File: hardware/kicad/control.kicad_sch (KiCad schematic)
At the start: 5 parts, among them SW1 MIDI channel, U9 Teensy 4.0

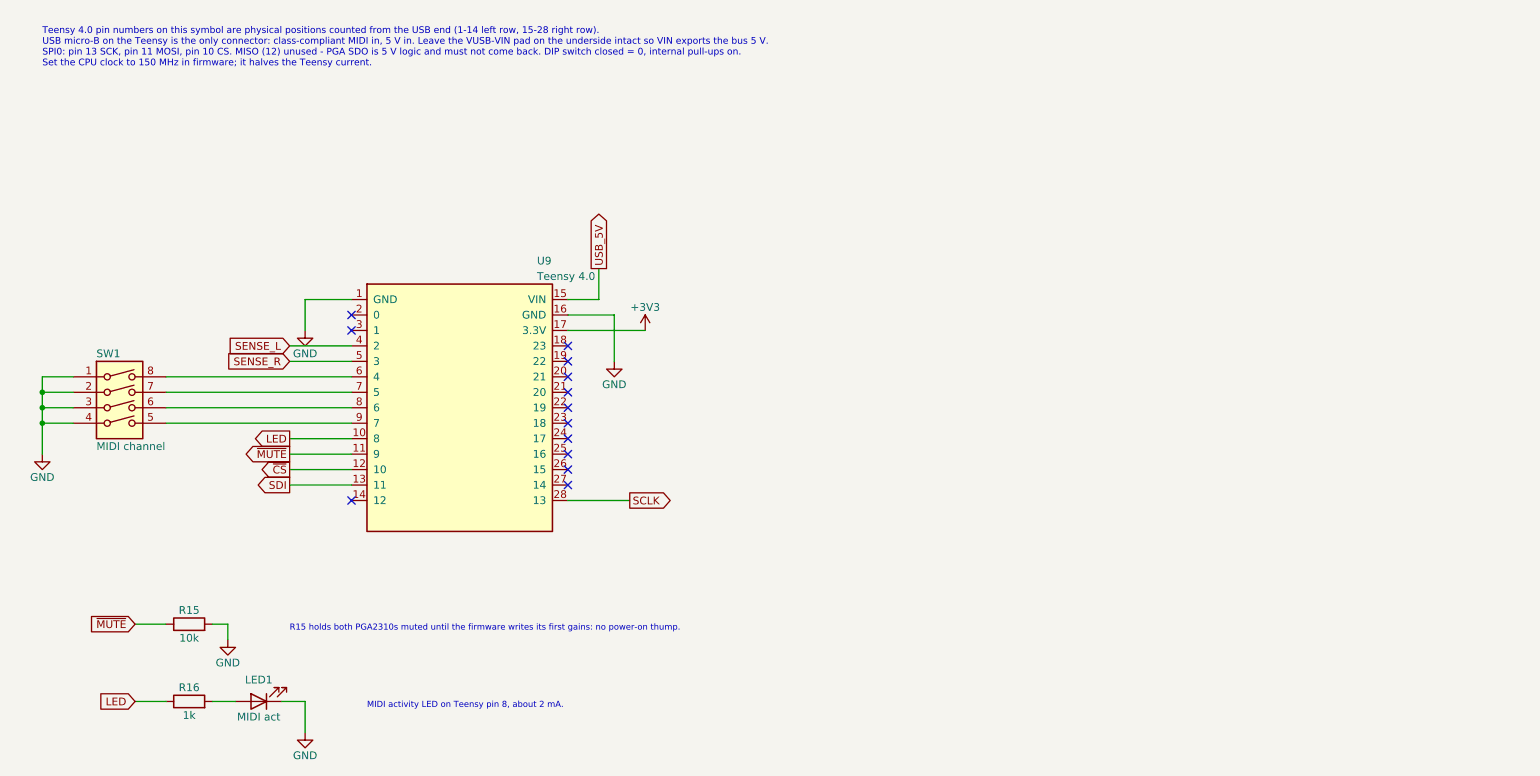
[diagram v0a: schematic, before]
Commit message: Rev C: XIAO RP2040 and Traco TBA 2-0522 replace the Teensy 4.0 and TMR 3
Tier 1 cost-down, no change to the audio path. U9 becomes a Seeed XIAO
RP2040 on header pins (USB-C, TinyUSB MIDI, its 5V pin is VBUS straight
through), PS1 becomes a 2 W unregulated Traco TBA 2-0522 on KiCad's stock
SIP-7 footprint. Rails are now +/-12 V: the +/-15 V TBA 2-0523 would pass
the PGA2310's 16 V absolute maximum at light load. Parts cost drops from
about $145 to about $110.

- gen.py: TBA2_Dual and XIAO_RP2040 symbols, XIAO footprint (Seeed pin
  numbering, USB-C overhang drawn), control sheet rewired to D0-D10,
  power sheet and notes for the unregulated converter, +/-12V rails.
- check.py: new U9 / PS1 pins; NETLIST OK. ERC 0/0.
- Both boards rebuilt and re-routed (Freerouting 1.9), DRC 0 errors; the
  only warnings are jack-nose and USB-C shell silk over the board edge.
- Gerbers, drill, zips, BOM, schematic SVG/PDF and board renders
  regenerated. README and site updated: pin map, power budget
  (~250 mA typical), level budget at +/-12 V, parts list and totals.

Co-Authored-By: Claude Fable 5.1 <noreply@anthropic.com>
Claude-Session: https://claude.ai/code/session_01C8uqpe49go1TPWMsWKKVkn
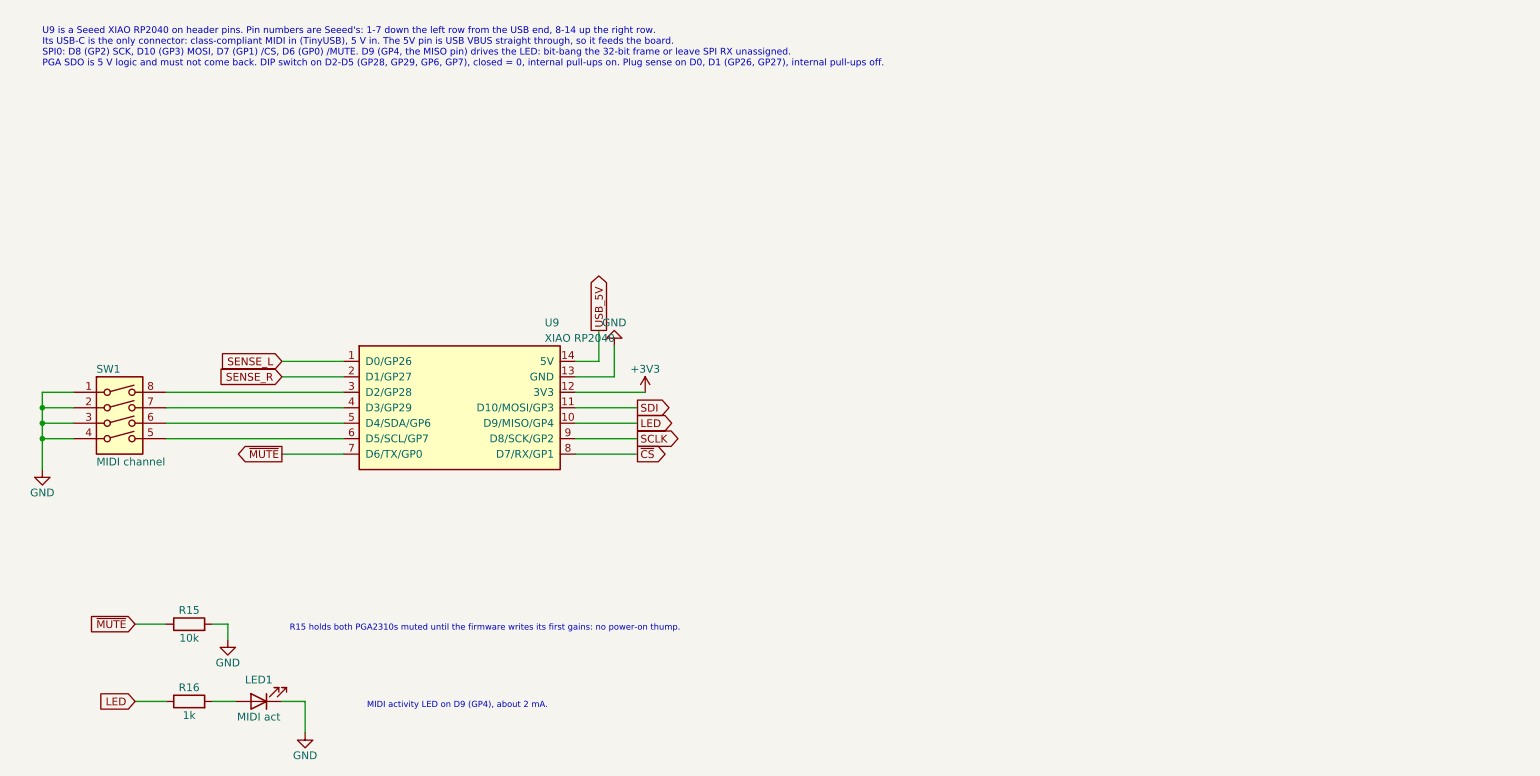
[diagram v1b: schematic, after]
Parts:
- removed U9: Teensy 4.0, GhostFader:Teensy40_Edge, symbol GhostFader:Teensy40
- added U9: XIAO RP2040, GhostFader:XIAO_RP2040_THT, symbol GhostFader:XIAO_RP2040
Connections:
- net +3V3: now also U9.12 (3V3)
- net GND: now also U9.13 (GND)
- net LED: now also U9.10 (D9/MISO/GP4)
- net SCLK: now also U9.9 (D8/SCK/GP2)
- net SDI: now also U9.11 (D10/MOSI/GP3)
- net SENSE_L: now also U9.1 (D0/GP26)
- net SENSE_R: now also U9.2 (D1/GP27)
- net USB_5V: now also U9.14 (5V)
- net ~{CS}: now also U9.8 (D7/RX/GP1)
- net ~{MUTE}: now also U9.7 (D6/TX/GP0)
- net at SW1.5: now also U9.6 (D5/SCL/GP7)
- net at SW1.6: now also U9.5 (D4/SDA/GP6)
- net at SW1.7: now also U9.4 (D3/GP29)
- net at SW1.8: now also U9.3 (D2/GP28)
- no-connect marks 13 -> 0
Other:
- note added: "MIDI activity LED on D9 (GP4), about 2 mA."
- note added: "U9 is a Seeed XIAO RP2040 on header pins. Pin numbers are Seeed's: 1-7 down the left row from the USB end, 8-14 up the right row. Its USB-C is the only connector: class-compliant MIDI in (TinyUSB), 5 V in. The 5V pin is USB VBUS straight through, so it feeds the board. SPI0: D8 (GP2) SCK, D10 (GP3) MOSI, D7 (GP1) /CS, D6 (GP0) /MUTE. D9 (GP4, the MISO pin) drives the LED: bit-bang the 32-bit fram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"
- note removed: "MIDI activity LED on Teensy pin 8, about 2 mA."
- note removed: "Teensy 4.0 pin numbers on this symbol are physical positions counted from the USB end (1-14 left row, 15-28 right row). USB micro-B on the Teensy is the only connector: class-compliant MIDI in, 5 V in. Leave the VUSB-VIN pad on the underside intact so VIN exports the bus 5 V. SPI0: pin 13 SCK, pin 11 MOSI, pin 10 CS. MISO (12) unused - PGA SDO is 5 V logic and must not come back. DIP switch close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"

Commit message: Rev D: isolate the audio ground from USB
Add a TI ISO7762FDW digital isolator on the four control lines and two
plug-sense lines, a 78L05 that makes +5VA from +12 V for the PGA logic
and the isolator's audio side, and a split ground: GND_USB (XIAO, USB-C,
switch, LED, ferrite, reservoir, DC-DC input) and GND (everything audio).
The two meet only through C45 (1 nF) and R17 (1 M) at PS1. The sense
pull-ups drop from 1 M to 100 k for the isolator's input leakage.

Both boards get two ground pours per layer with a 2 mm copper-free gap
and a rule area that keeps the router out; U8 and PS1 straddle the gap.
The 1590BB board's island is the front-left corner; the narrow board's
is a pocket under the XIAO with the audio ground wrapping beneath it.
ERC 0, netlist checked (61 nets, 263 pins), DRC clean on both routed
boards, and a script check confirms no copper crosses the gap.

README, docs page, schematic exports, renders, gerbers and BOM regenerated.

Co-Authored-By: Claude Fable 5.1 <noreply@anthropic.com>
Claude-Session: https://claude.ai/code/session_013C8baRPktSQjwfdzSRwmAq
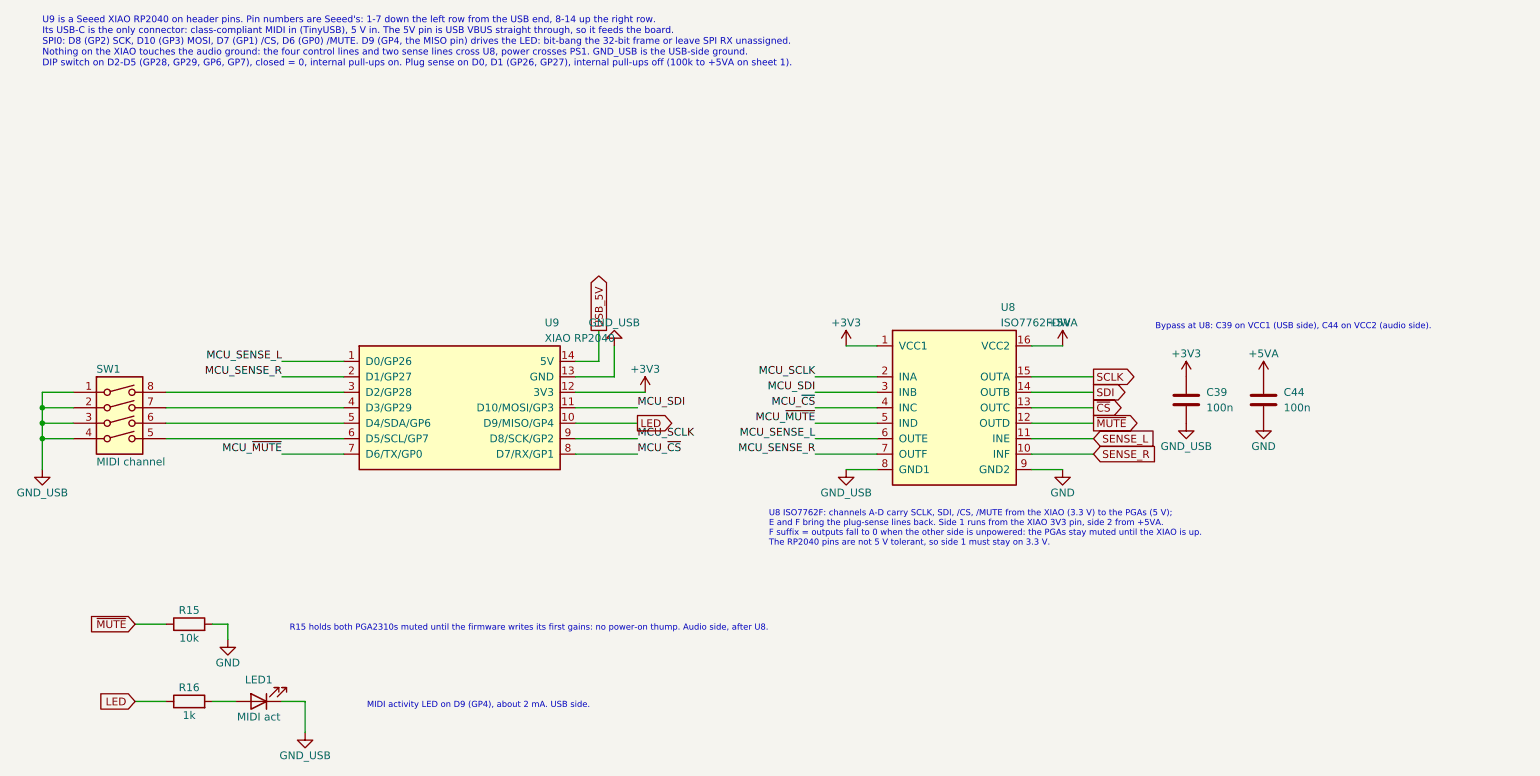
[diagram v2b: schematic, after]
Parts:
- added C39, C44: 100n, Capacitor_THT:C_Disc_D5.0mm_W2.5mm_P5.00mm, symbol Device:C
- added U8: ISO7762FDW, Package_SO:SOIC-16W_7.5x10.3mm_P1.27mm, symbol GhostFader:ISO7762F
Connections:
- net +3V3: now also C39.1, U8.1 (VCC1)
- net GND: now also C44.2, U8.9 (GND2); no longer LED1.1 (K), SW1.1, SW1.2, SW1.3, SW1.4, U9.13 (GND)
- net SCLK: now also U8.15 (OUTA); no longer U9.9 (D8/SCK/GP2)
- net SDI: now also U8.14 (OUTB); no longer U9.11 (D10/MOSI/GP3)
- net SENSE_L: now also U8.11 (INE); no longer U9.1 (D0/GP26)
- net SENSE_R: now also U8.10 (INF); no longer U9.2 (D1/GP27)
- net ~{CS}: now also U8.13 (OUTC); no longer U9.8 (D7/RX/GP1)
- net ~{MUTE}: now also U8.12 (OUTD); no longer U9.7 (D6/TX/GP0)
- new net +5VA: C44.1, U8.16 (VCC2)
- new net GND_USB: C39.2, LED1.1 (K), SW1.1, SW1.2, SW1.3, SW1.4, U8.8 (GND1), U9.13 (GND)
- new net MCU_SCLK: U8.2 (INA), U9.9 (D8/SCK/GP2)
- new net MCU_SDI: U8.3 (INB), U9.11 (D10/MOSI/GP3)
- new net MCU_SENSE_L: U8.6 (OUTE), U9.1 (D0/GP26)
- new net MCU_SENSE_R: U8.7 (OUTF), U9.2 (D1/GP27)
- new net MCU_~{CS}: U8.4 (INC), U9.8 (D7/RX/GP1)
- new net MCU_~{MUTE}: U8.5 (IND), U9.7 (D6/TX/GP0)
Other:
- note added: "Bypass at U8: C39 on VCC1 (USB side), C44 on VCC2 (audio side)."
- note added: "MIDI activity LED on D9 (GP4), about 2 mA. USB side."
- note added: "R15 holds both PGA2310s muted until the firmware writes its first gains: no power-on thump. Audio side, after U8."
- note added: "U8 ISO7762F: channels A-D carry SCLK, SDI, /CS, /MUTE from the XIAO (3.3 V) to the PGAs (5 V); E and F bring the plug-sense lines back. Side 1 runs from the XIAO 3V3 pin, side 2 from +5VA. F suffix = outputs fall to 0 when the other side is unpowered: the PGAs stay muted until the XIAO is up. The RP2040 pins are not 5 V tolerant, so side 1 must stay on 3.3 V."
- note removed: "MIDI activity LED on D9 (GP4), about 2 mA."
- note removed: "R15 holds both PGA2310s muted until the firmware writes its first gains: no power-on thump."
